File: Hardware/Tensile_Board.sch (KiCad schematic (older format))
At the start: 27 parts, among them J1 Conn_02x05_Odd_Even, J11 Screw_Terminal_01x04, J2 Conn_02x05_Odd_Even, J3 Conn_02x05_Odd_Even, J4 Conn_02x05_Odd_Even, J5 Micro_SD_Card, J6 Main_Power, J9 Grounding, U1 AMS1117-5.0, U2 AMS1117-3.3, U20 APM4953, U3 DS3231M

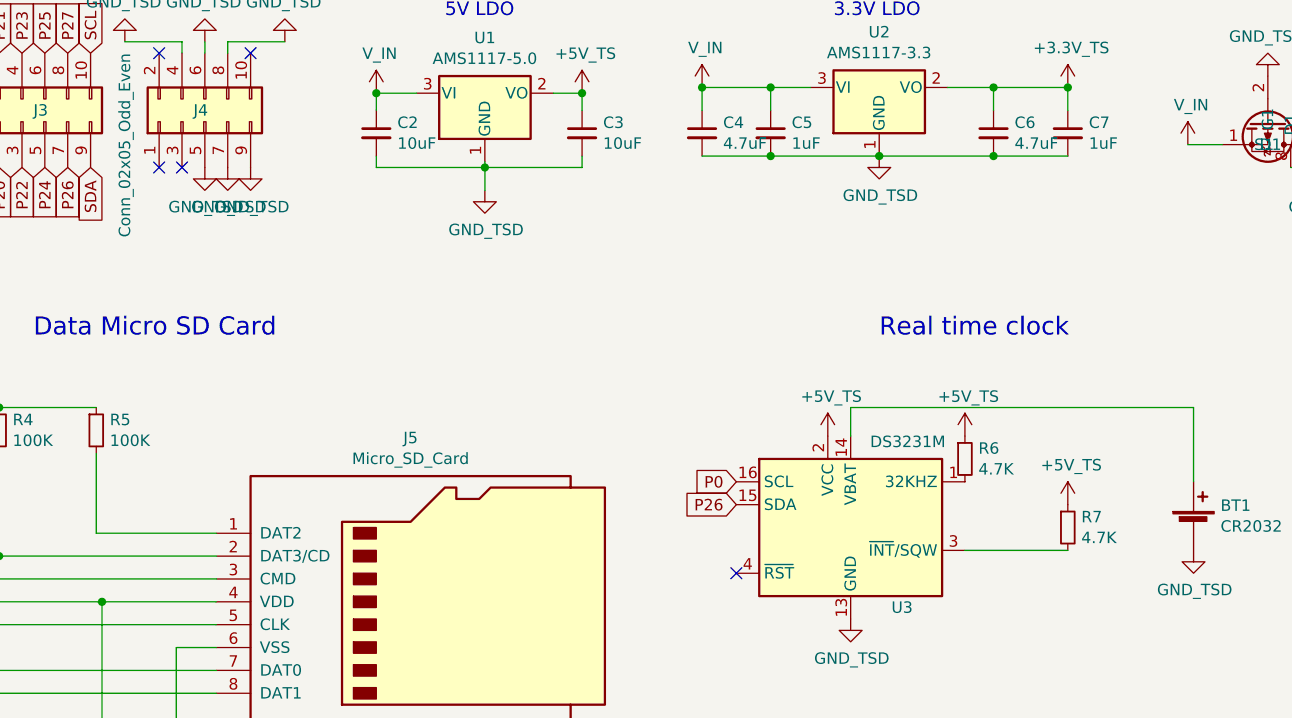
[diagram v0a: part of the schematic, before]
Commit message: fixed silk screen issues with rev_1
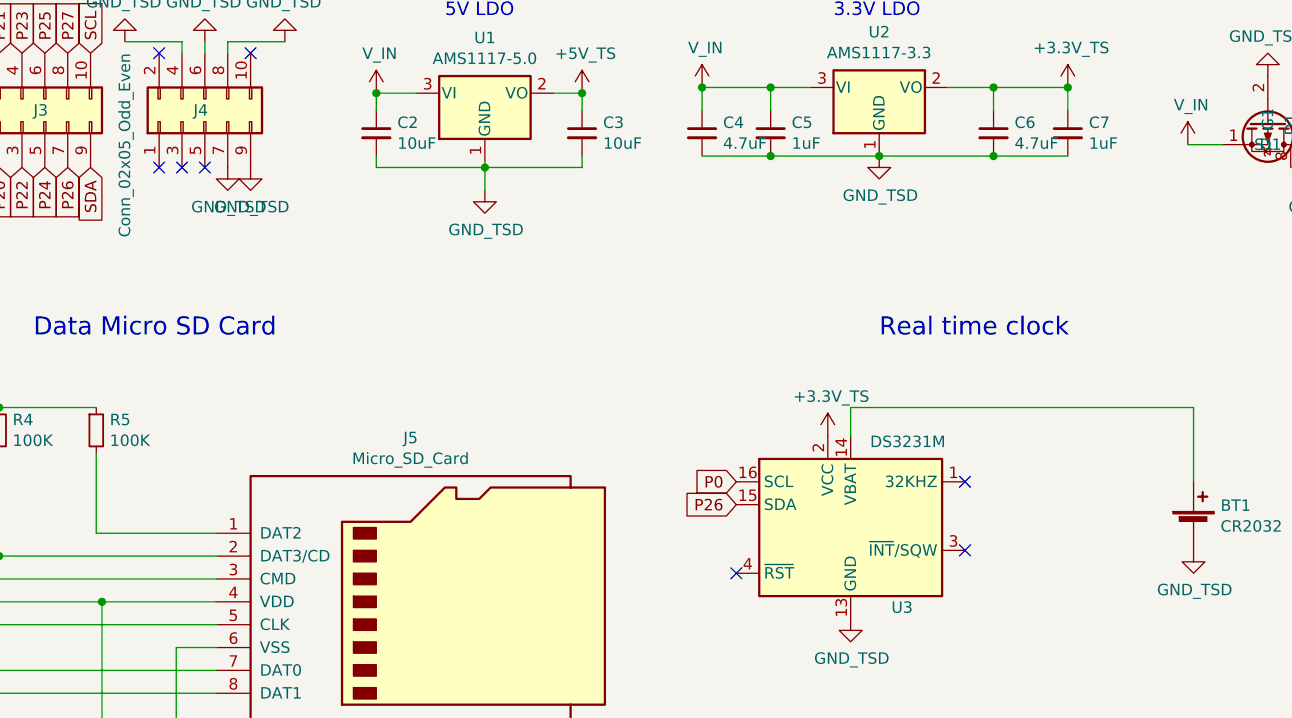
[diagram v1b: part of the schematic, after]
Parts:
- removed R6, R7: 4.7K, Resistor_SMD:R_0603_1608Metric, symbol Device:R_Small
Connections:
- net +3V3_TS: now also U3.2 (VCC)
- net +5V_TS: no longer U3.2 (VCC)
- net GND_TSD: no longer J4.5 (Pin_5)
- no-connect marks 5 -> 8
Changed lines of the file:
@@
-	1    0    0    -1
-$EndComp
-$Comp
-L Tensile_Board:GND_TSD #PWR0285
-U 1 1 606FDD28
-P 3100 1600
-F 0 "#PWR0285" H 3100 1350 50  0001 C CNN
-F 1 "GND_TSD" H 3105 1427 50  0000 C CNN
-F 2 "" H 3100 1600 50  0001 C CNN
-F 3 "" H 3100 1600 50  0001 C CNN
-	1    3100 1600
 	1    0    0    -1
 $EndComp
@@
 Wire Wire Line
 	5925 2775 5925 2650
-Wire Wire Line
-	6425 3275 6875 3275
-$Comp
-L Tensile_Board:+5V_TS #PWR0112
-U 1 1 601A798A
-P 6875 3075
-F 0 "#PWR0112" H 6875 2925 50  0001 C CNN
-F 1 "+5V_TS" H 6890 3248 50  0000 C CNN
-F 2 "" H 6875 3075 50  0001 C CNN
-F 3 "" H 6875 3075 50  0001 C CNN
-	1    6875 3075
-	1    0    0    -1
-$EndComp
-$Comp
-L Tensile_Board:+5V_TS #PWR0111
-U 1 1 601A7204
-P 6425 2775
-F 0 "#PWR0111" H 6425 2625 50  0001 C CNN
-F 1 "+5V_TS" H 6440 2948 50  0000 C CNN
-F 2 "" H 6425 2775 50  0001 C CNN
-F 3 "" H 6425 2775 50  0001 C CNN
-	1    6425 2775
-	1    0    0    -1
-$EndComp
-$Comp
-L Device:R_Small R7
-U 1 1 601A6225
-P 6875 3175
-F 0 "R7" H 6934 3221 50  0000 L CNN
-F 1 "4.7K" H 6934 3130 50  0000 L CNN
-F 2 "Resistor_SMD:R_0603_1608Metric" H 6875 3175 50  0001 C CNN
-F 3 "https://datasheet.lcsc.com/szlcsc/Uniroyal-Elec-0603WAF4701T5E_C23162.pdf" H 6875 3175 50  0001 C CNN
-F 4 "C23162" H 6875 3175 50  0001 C CNN "LCSC"
-F 5 "BASIC" H 6875 3175 50  0001 C CNN "Type"
-	1    6875 3175
-	1    0    0    -1
-$EndComp
-$Comp
-L Device:R_Small R6
-U 1 1 601A5164
-P 6425 2875
-F 0 "R6" H 6484 2921 50  0000 L CNN
-F 1 "4.7K" H 6484 2830 50  0000 L CNN
-F 2 "Resistor_SMD:R_0603_1608Metric" H 6425 2875 50  0001 C CNN
-F 3 "https://datasheet.lcsc.com/szlcsc/Uniroyal-Elec-0603WAF4701T5E_C23162.pdf" H 6425 2875 50  0001 C CNN
-F 4 "C23162" H 6425 2875 50  0001 C CNN "LCSC"
-F 5 "BASIC" H 6425 2875 50  0001 C CNN "Type"
-	1    6425 2875
-	1    0    0    -1
-$EndComp
 Text GLabel 5425 3075 0    50   Input ~ 0
 P26
@@
 Text Notes 6050 2350 0    79   ~ 0
 Real time clock
-$Comp
-L Tensile_Board:+5V_TS #PWR0110
-U 1 1 6023FC7A
-P 5825 2775
-F 0 "#PWR0110" H 5825 2625 50  0001 C CNN
-F 1 "+5V_TS" H 5840 2948 50  0000 C CNN
-F 2 "" H 5825 2775 50  0001 C CNN
-F 3 "" H 5825 2775 50  0001 C CNN
-	1    5825 2775
-	1    0    0    -1
-$EndComp
 $Comp
 L Tensile_Board:GND_TSD #PWR0109
@@
 Wire Wire Line
 	3100 1050 3100 1100
+NoConn ~ 3100 1600
+$Comp
+L Tensile_Board:+3.3V_TS #PWR0110
+U 1 1 6047F84C
+P 5825 2775
+F 0 "#PWR0110" H 5825 2625 50  0001 C CNN
+F 1 "+3.3V_TS" H 5840 2948 50  0000 C CNN
+F 2 "" H 5825 2775 50  0001 C CNN
+F 3 "" H 5825 2775 50  0001 C CNN
+	1    5825 2775
+	1    0    0    -1
+$EndComp
+NoConn ~ 6425 2975
+NoConn ~ 6425 3275
 $EndSCHEMATC
